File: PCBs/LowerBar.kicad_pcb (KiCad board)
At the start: 2 copper layers, 144.8 x 34.3 mm, 12 parts, among them J2 8 Pin Connector, SW18 SW_SPST, SW19 SW_SPST, SW20 SW_SPST, SW21 SW_SPST, SW22 SW_SPST, SW23 SW_SPST, SW24 SW_SPST

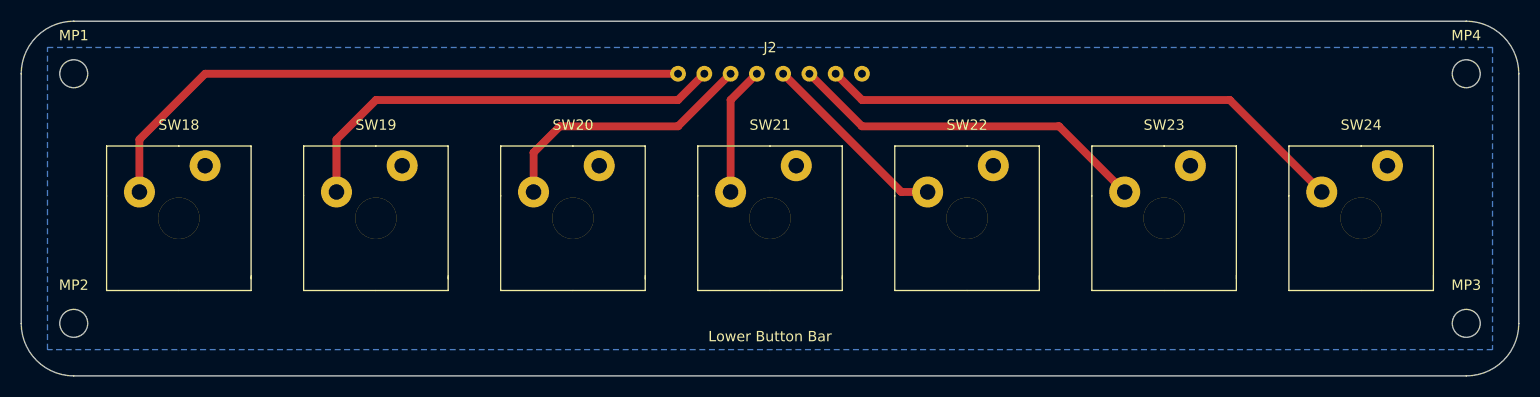
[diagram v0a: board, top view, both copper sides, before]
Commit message: Routed back side board
Routed the LED drivers, pin headers, shift registers, etc. that are on the back side. ECAD is close to done, and I will start on the MCAD at this point.
-Decided to avoid routing anodes and common cathodes to each of the comm channel displays, as that would probably have required at least an extra layer, instead I added a header to plug crimped wires directly into the front side.
-Some of the headers are two single width pin headers put side by side, meaning their courtyards overlap. I may redo this to use one footprint for both in the future.
-Still undecided on a couple part values
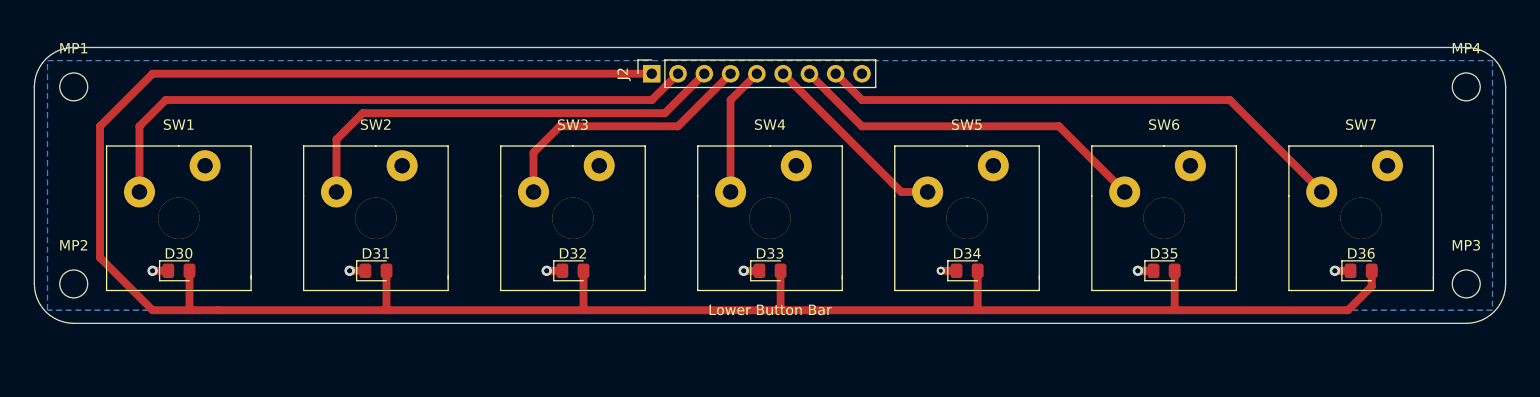
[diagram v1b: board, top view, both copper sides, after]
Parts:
- added D30: LED, LED_SMD:LED_0805_2012Metric_Pad1.15x1.40mm_HandSolder, F.Cu at (127.0, 74.9)
- added D31: LED, LED_SMD:LED_0805_2012Metric_Pad1.15x1.40mm_HandSolder, F.Cu at (146.1, 74.9)
- added D32: LED, LED_SMD:LED_0805_2012Metric_Pad1.15x1.40mm_HandSolder, F.Cu at (165.1, 74.9)
- added D33: LED, LED_SMD:LED_0805_2012Metric_Pad1.15x1.40mm_HandSolder, F.Cu at (184.2, 74.9)
- added D34: LED, LED_SMD:LED_0805_2012Metric_Pad1.15x1.40mm_HandSolder, F.Cu at (203.2, 74.9)
- added D35: LED, LED_SMD:LED_0805_2012Metric_Pad1.15x1.40mm_HandSolder, F.Cu at (222.2, 74.9)
- added D36: LED, LED_SMD:LED_0805_2012Metric_Pad1.15x1.40mm_HandSolder, F.Cu at (241.3, 74.9)
- J2: value 8 Pin Connector -> 9pin; footprint UFC:8pin254mm -> Connector_PinSocket_2.54mm:PinSocket_1x09_P2.54mm_Vertical
- moved J2 11.5 mm to (172.7, 55.9), turned to 90 degrees
- moved MP2 3.81 mm to (116.8, 76.2)
- moved MP3 3.81 mm to (251.5, 76.2)
- moved MP1 1.27 mm to (116.8, 57.1)
- moved MP4 1.27 mm to (251.5, 57.1)
- renumbered SW18 to SW1, SW19 to SW2, SW20 to SW3, SW21 to SW4, SW22 to SW5, SW23 to SW6, SW24 to SW7
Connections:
- J2 pad 1: /GND -> /LED
- J2 pad 2: /SW24 -> /SW18
- J2 pad 3: /SW23 -> /SW19
- J2 pad 4: /SW22 -> /SW20
- J2 pad 6: /SW20 -> /SW22
- J2 pad 7: /SW19 -> /SW23
- J2 pad 8: /SW18 -> /SW24
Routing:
- net /LED: track 0.00 -> 219.1 mm
- net /GND: track 0.00 -> 10.6 mm, vias 0 -> 7
- net /SW18: track 59.8 -> 60.5 mm
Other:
- board size 144.8 x 34.3 mm -> 142.2 x 26.7 mm
- board text added: "TAC UFC BUTTON BAR"

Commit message: Removed comm displays from PCB
Since they will be connected with wires anyways it didn't make sense to keep them on.
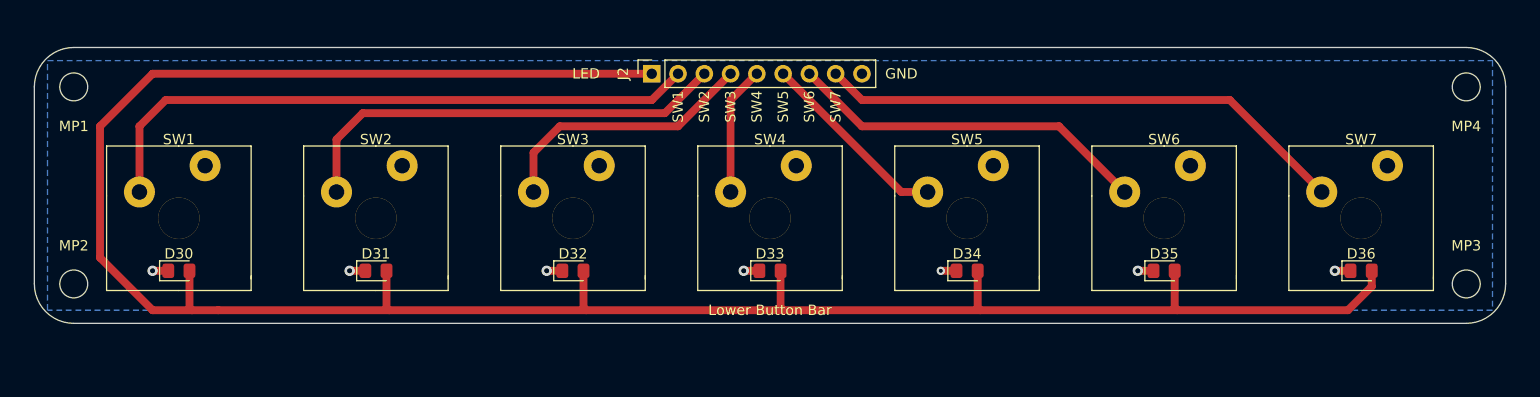
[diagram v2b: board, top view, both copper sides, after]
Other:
- board text added: "GND"
- board text added: "LED"
- board text added: "SW1"
- board text added: "SW2"
- board text added: "SW3"
- board text added: "SW4"
- board text added: "SW5"
- board text added: "SW6"
- board text added: "SW7"

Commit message: Updated PCBs, cleaned up files
No commit for a while; a lot has happened in the mean time. JLC refused my order for the display layers, so I settled for just the dot layer. The gerbers for the rest are deleted, but the kicad files are still present.

I also received the main PCBs from JLC, and edited a couple small details.
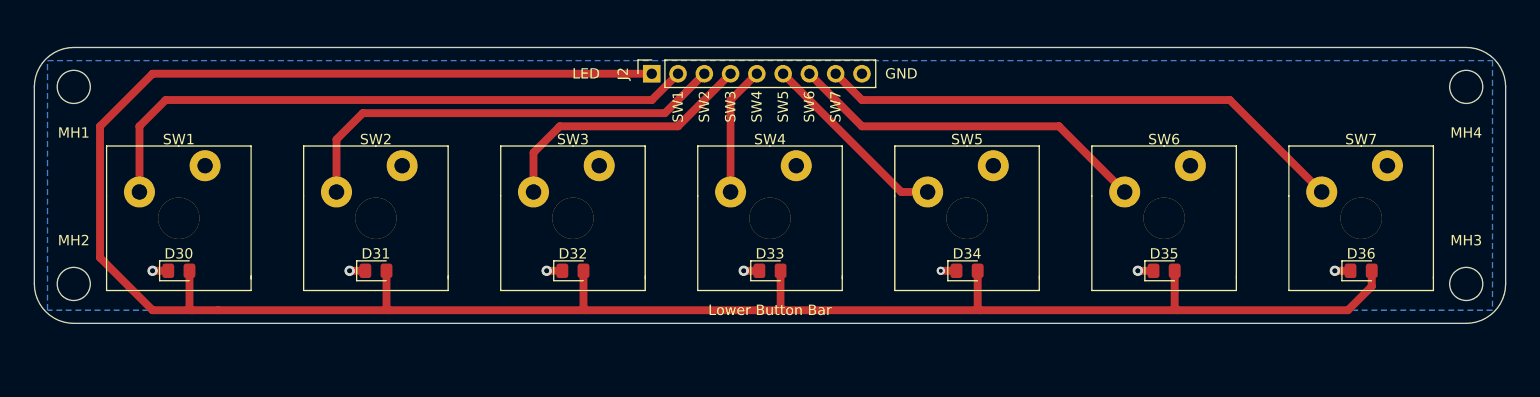
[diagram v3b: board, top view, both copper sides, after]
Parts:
- removed MP1, MP2, MP3, MP4: M2.5, MountingHole:MountingHole_2.7mm_M2.5
- added MH1: M3, MountingHole:MountingHole_3.2mm_M3, F.Cu at (116.8, 57.1)
- added MH2: M3, MountingHole:MountingHole_3.2mm_M3, F.Cu at (116.8, 76.2)
- added MH3: M3, MountingHole:MountingHole_3.2mm_M3, F.Cu at (251.5, 76.2)
- added MH4: M3, MountingHole:MountingHole_3.2mm_M3, F.Cu at (251.5, 57.1)

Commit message: Fixed design error
Untested as of now.
Removed direct connection from PWM out to LEDs, as the PWM pins on the bluepill can't provide enough current. Added P channel mosfet, and individual resistors per parallel LED. For now, the single resistor for all LEDs is still present, but bypassable via jumper, for the sake of backwards compatibility.
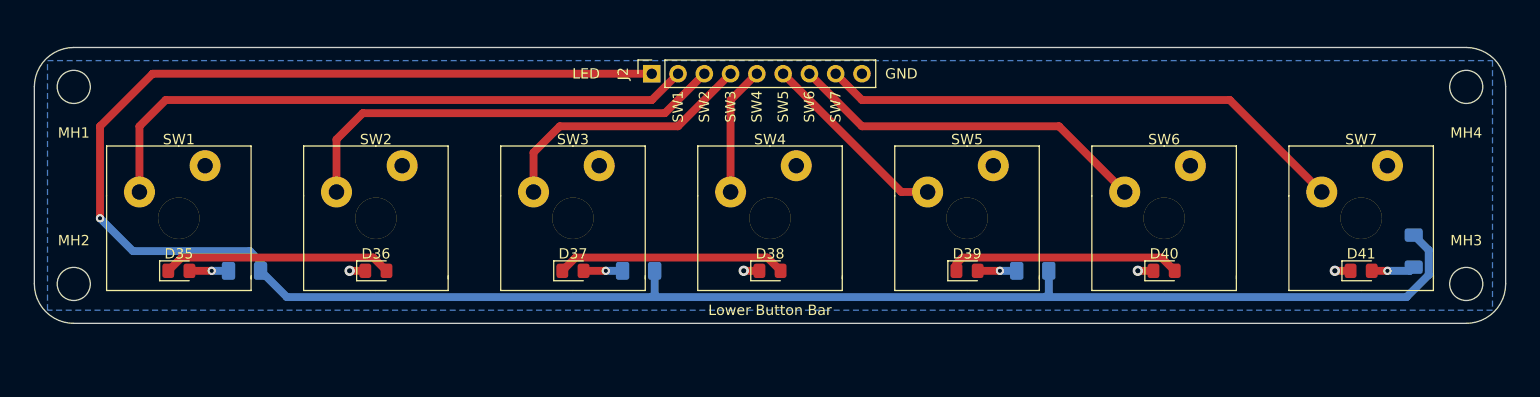
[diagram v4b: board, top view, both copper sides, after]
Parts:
- added R46: 100R, Resistor_SMD:R_1206_3216Metric_Pad1.30x1.75mm_HandSolder, B.Cu at (133.3, 74.9)
- added R47: 100R, Resistor_SMD:R_1206_3216Metric_Pad1.30x1.75mm_HandSolder, B.Cu at (171.4, 74.9)
- added R48: 100R, Resistor_SMD:R_1206_3216Metric_Pad1.30x1.75mm_HandSolder, B.Cu at (209.6, 74.9)
- added R49: 300R, Resistor_SMD:R_1206_3216Metric_Pad1.30x1.75mm_HandSolder, B.Cu at (246.4, 73.0)
- SW1, SW2, SW3, SW4, SW5, SW6, SW7: value SW_SPST -> KeySW
- renumbered D30 to D35, D31 to D36, D32 to D37, D33 to D38, D34 to D39, D35 to D40, D36 to D41
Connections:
- D35 pad 1: /GND -> Net-(D35-Pad1)
- D35 pad 2: /LED -> Net-(D35-Pad2)
- D36 pad 2: /LED -> Net-(D35-Pad1)
- D37 pad 1: /GND -> Net-(D37-Pad1)
- D37 pad 2: /LED -> Net-(D37-Pad2)
- D38 pad 2: /LED -> Net-(D37-Pad1)
- D39 pad 1: /GND -> Net-(D39-Pad1)
- D39 pad 2: /LED -> Net-(D39-Pad2)
- D40 pad 2: /LED -> Net-(D39-Pad1)
- D41 pad 2: /LED -> Net-(D41-Pad2)
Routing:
- net Net-(D39-Pad1): track 0.00 -> 22.6 mm
- net Net-(D37-Pad1): track 0.00 -> 22.2 mm
- net Net-(D35-Pad1): track 0.00 -> 22.2 mm
- net /LED: track 219.1 -> 207.1 mm, vias 0 -> 1
- net /GND: track 10.6 -> 6.06 mm, vias 7 -> 4
- net Net-(D41-Pad2): track 0.00 -> 4.20 mm, vias 0 -> 1
- net Net-(D39-Pad2): track 0.00 -> 3.78 mm, vias 0 -> 1
- net Net-(D37-Pad2): track 0.00 -> 3.78 mm, vias 0 -> 1
- net Net-(D35-Pad2): track 0.00 -> 3.78 mm, vias 0 -> 1
